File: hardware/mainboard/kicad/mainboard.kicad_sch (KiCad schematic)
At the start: 0 parts

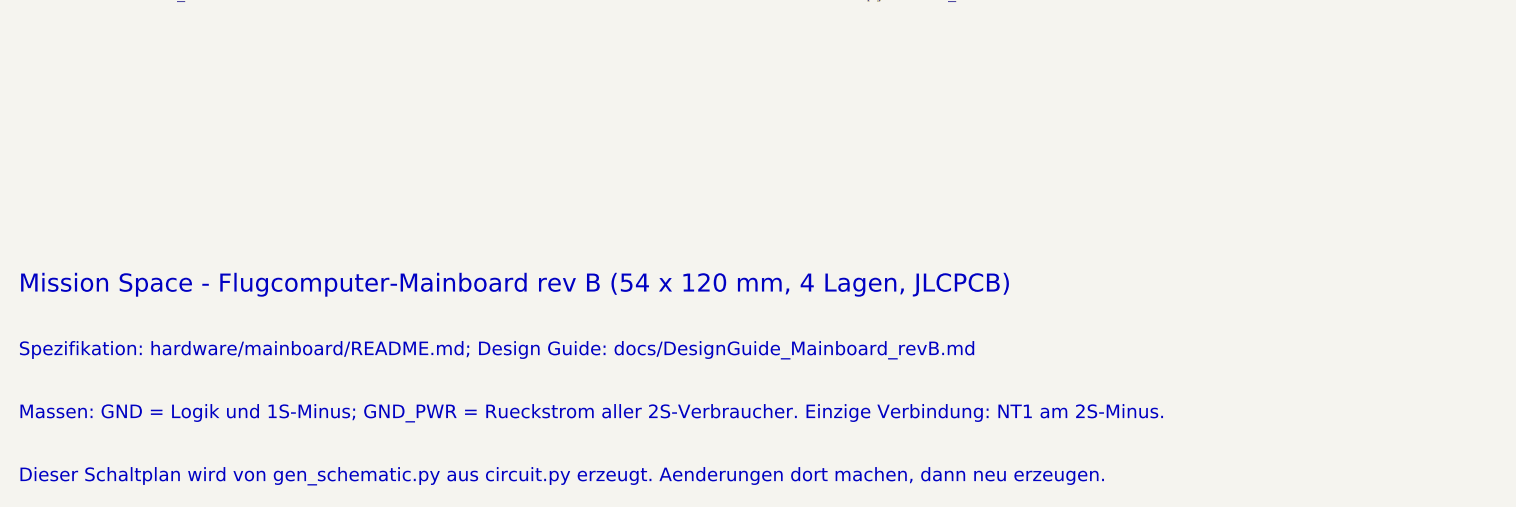
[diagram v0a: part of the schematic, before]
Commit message: Kartonaut: Name, Missionsabzeichen, Bestückungsdruck neu, Lötstopp blau
- Projekt heißt Kartonaut (Karton + Astronaut); Flüge werden hochgezählt, Erstflug = Kartonaut 1
- Abzeichen als Polygone in hardware/mainboard/kicad/logo.py, SVGs in docs/brand/
- spacecode/ -> firmware/, Bodenstation-Repo groundcode -> kartonaut-ground (Links, .gitignore)
- gen_pcb.py silk: Bestückungsdruck nur neu setzen, auf der gerouteten Platine; 1,0 mm Schrift,
  freie Plätze statt Überlappungen, Kurznamen an den Steckern, Testpunkte mit Netznamen,
  kleines Abzeichen vorn; hinten Abzeichen 20 mm und Steckerbelegung
- Stackup JLC04161H-7628 mit blauem Lötstopp im Board, Renders mit Stackup-Farben
- DRC-Druckwarnungen 167 -> 14 (Rest aus Footprint-Umrissen)

Co-Authored-By: Claude Opus 5.5 <noreply@anthropic.com>
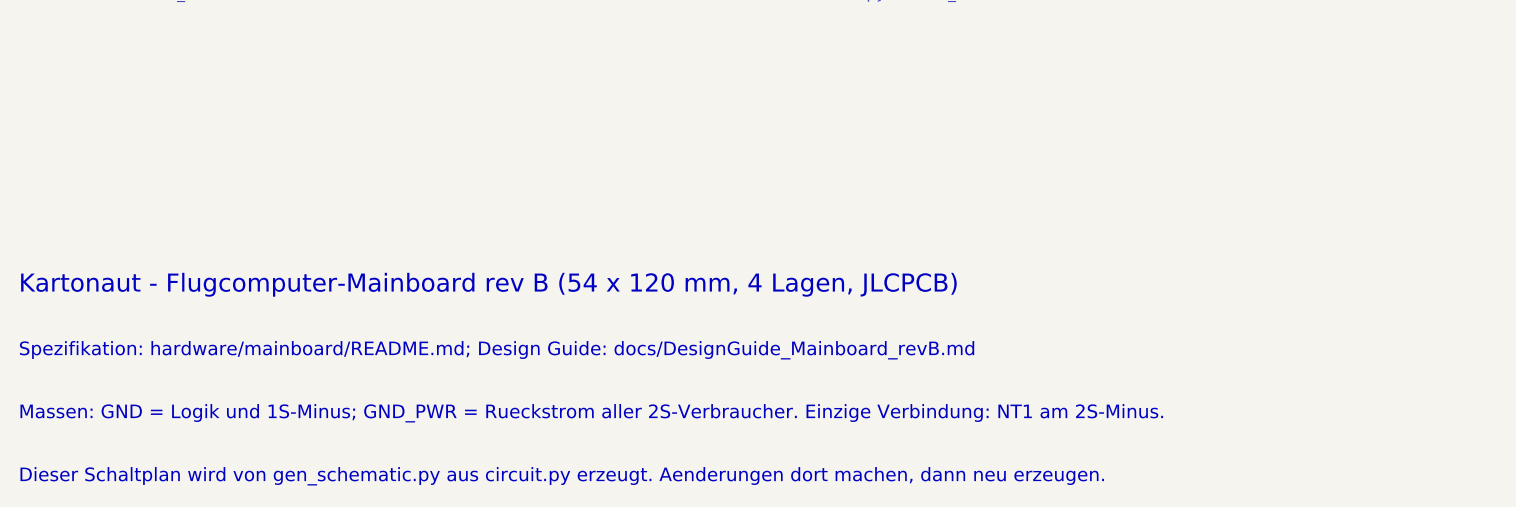
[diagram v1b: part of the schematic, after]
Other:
- note added: "Kartonaut - Flugcomputer-Mainboard rev B (54 x 120 mm, 4 Lagen, JLCPCB)"
- note removed: "Mission Space - Flugcomputer-Mainboard rev B (54 x 120 mm, 4 Lagen, JLCPCB)"
- company: Mission Space -> Kartonaut
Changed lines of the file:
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@@
 		(date "2026-10-21")
 		(rev "B")
-		(company "Mission Space")
+		(company "Kartonaut")
 		(comment 1 "Teensy 4.1, ICM-42688-P, BMP390, E22-400T22S, 1S + 2S")
 	)
@@
 		(effects (font (size 1.27 1.27)) (justify left top))
 	)
-	(text "Mission Space - Flugcomputer-Mainboard rev B (54 x 120 mm, 4 Lagen, JLCPCB)"
+	(text "Kartonaut - Flugcomputer-Mainboard rev B (54 x 120 mm, 4 Lagen, JLCPCB)"
 		(exclude_from_sim no)
 		(at 30 180 0)

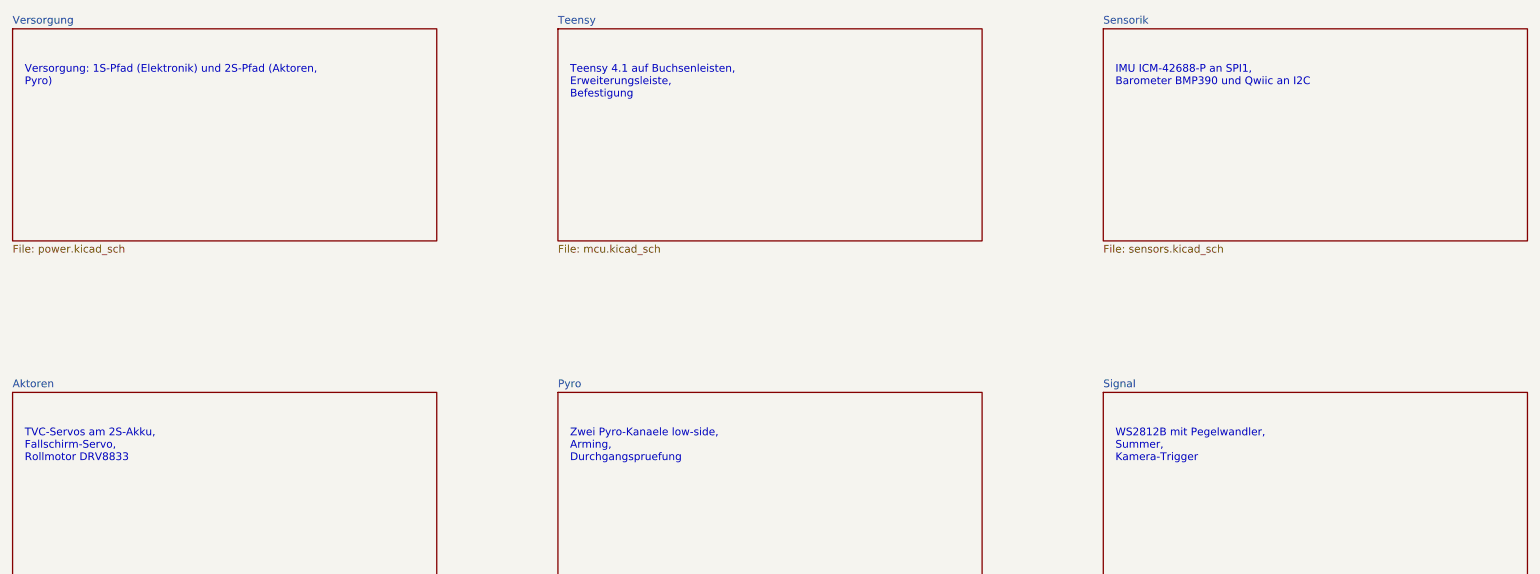
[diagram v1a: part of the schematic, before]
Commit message: Mainboard rev B1: Review A1-A8 und Entscheidungen E1-E10 eingearbeitet, 2S-Pfad als F.Cu-Flaechen, 28 Verbindungen offen
Schaltung (circuit.py, ERC 0, Netzliste gegen README §4 OK): Hold-up hinter D1, EN-Teiler 330k/115k,
P-FET-Lastschalter je Akku, Polyfuse je Akku, Kelvin-Shunt mit INA239 an SPI1, BMP390 an SPI1,
74HC138/74HC4051 mit gemeinsamer Adresse, J_STACK 2x10 mit LDO 3V3_EXP, 1S-Lader MCP73831,
J_CHG2, vier Pyro-Kanaele (3/4 DNP), vierter Servo, alle Servos und Rollmotor an VSERVO,
3V3_SENS, eine WS2812B-Kette, Summer Pin 37, E22 NRST Pin 6; 166 Bauteile.

Platine (gen_pcb.py): neue Platzierung, 2S-Pfad, Pyro-Ausgaenge und VSYS_IN als F.Cu-Flaechen mit
Sperrflaechen fuer Freerouting, Strom-Klasse nur F.Cu, IMU-Zone 5 mm, patch mit Umweg ueber In2.
DRC 0 Fehler, Paritaet 0, kein 2S-Netz auf In2; 28 offene Verbindungen, Liste in kicad/README.md §5.5.
Spezifikation README.md und kicad/README.md auf B1 nachgezogen, review_check_layout.py fuer B1.

Co-Authored-By: Claude Opus 5.5 <noreply@anthropic.com>
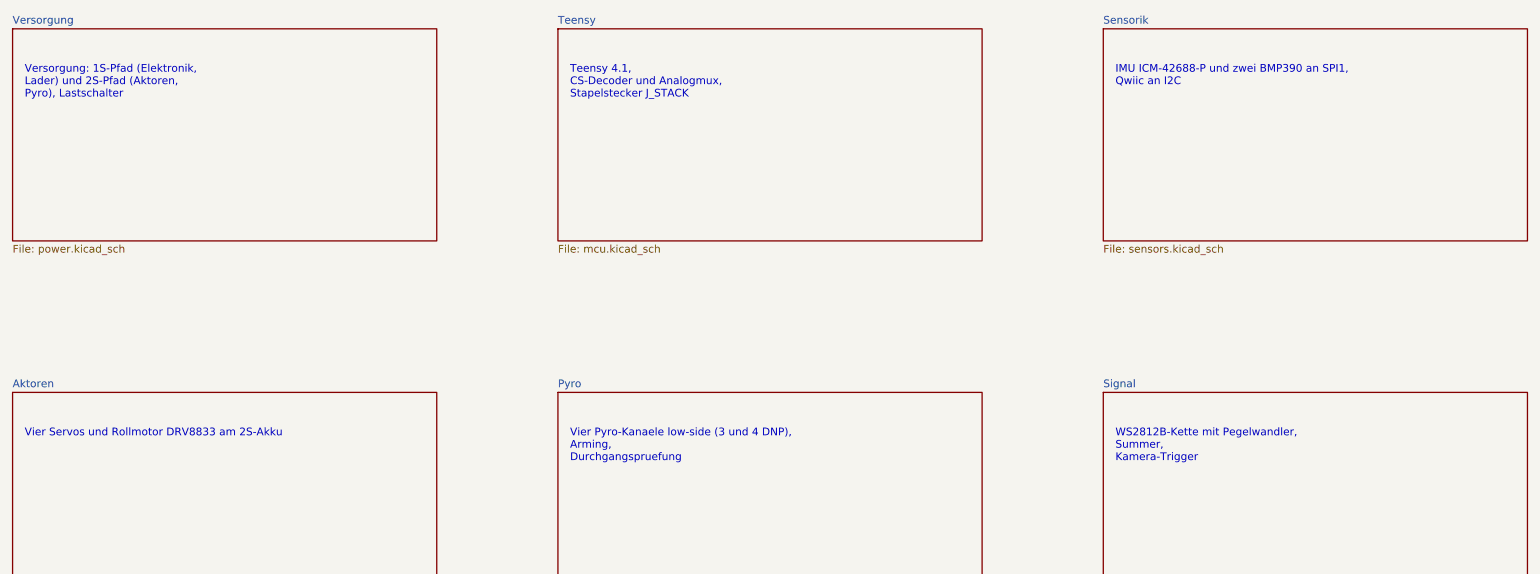
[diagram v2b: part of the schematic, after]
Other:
- note added: "IMU ICM-42688-P und zwei BMP390 an SPI1, Qwiic an I2C"
- note added: "Teensy 4.1, CS-Decoder und Analogmux, Stapelstecker J_STACK"
- note added: "Versorgung: 1S-Pfad (Elektronik, Lader) und 2S-Pfad (Aktoren, Pyro), Lastschalter"
- note added: "Vier Pyro-Kanaele low-side (3 und 4 DNP), Arming, Durchgangspruefung"
- note added: "Vier Servos und Rollmotor DRV8833 am 2S-Akku"
- note added: "WS2812B-Kette mit Pegelwandler, Summer, Kamera-Trigger"
- note removed: "IMU ICM-42688-P an SPI1, Barometer BMP390 und Qwiic an I2C"
- note removed: "TVC-Servos am 2S-Akku, Fallschirm-Servo, Rollmotor DRV8833"
- note removed: "Teensy 4.1 auf Buchsenleisten, Erweiterungsleiste, Befestigung"
- note removed: "Versorgung: 1S-Pfad (Elektronik) und 2S-Pfad (Aktoren, Pyro)"
- note removed: "WS2812B mit Pegelwandler, Summer, Kamera-Trigger"
- note removed: "Zwei Pyro-Kanaele low-side, Arming, Durchgangspruefung"
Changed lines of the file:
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@@
 		)
 	)
-	(text "Versorgung: 1S-Pfad (Elektronik) und 2S-Pfad (Aktoren,\nPyro)"
+	(text "Versorgung: 1S-Pfad (Elektronik,\nLader) und 2S-Pfad (Aktoren,\nPyro), Lastschalter"
 		(exclude_from_sim no)
 		(at 32 56 0)
@@
 		)
 	)
-	(text "Teensy 4.1 auf Buchsenleisten,\nErweiterungsleiste,\nBefestigung"
+	(text "Teensy 4.1,\nCS-Decoder und Analogmux,\nStapelstecker J_STACK"
 		(exclude_from_sim no)
 		(at 122 56 0)
@@
 		)
 	)
-	(text "IMU ICM-42688-P an SPI1,\nBarometer BMP390 und Qwiic an I2C"
+	(text "IMU ICM-42688-P und zwei BMP390 an SPI1,\nQwiic an I2C"
 		(exclude_from_sim no)
 		(at 212 56 0)
@@
 		)
 	)
-	(text "TVC-Servos am 2S-Akku,\nFallschirm-Servo,\nRollmotor DRV8833"
+	(text "Vier Servos und Rollmotor DRV8833 am 2S-Akku"
 		(exclude_from_sim no)
 		(at 32 116 0)
@@
 		)
 	)
-	(text "Zwei Pyro-Kanaele low-side,\nArming,\nDurchgangspruefung"
+	(text "Vier Pyro-Kanaele low-side (3 und 4 DNP),\nArming,\nDurchgangspruefung"
 		(exclude_from_sim no)
 		(at 122 116 0)
@@
 		)
 	)
-	(text "WS2812B mit Pegelwandler,\nSummer,\nKamera-Trigger"
+	(text "WS2812B-Kette mit Pegelwandler,\nSummer,\nKamera-Trigger"
 		(exclude_from_sim no)
 		(at 212 116 0)

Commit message: Schaltplan: Blattname Sensorik mit LSM6DSV16X auch im Wurzelblatt
Co-Authored-By: Claude Fable 5.1 <noreply@anthropic.com>
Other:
- note added: "IMU LSM6DSV16X und zwei BMP390 an SPI1, I2C-Sensoren und Qwiic"
- note removed: "IMU ICM-42688-P und zwei BMP390 an SPI1, Qwiic an I2C"
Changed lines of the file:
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@@
 		)
 	)
-	(text "IMU ICM-42688-P und zwei BMP390 an SPI1,\nQwiic an I2C"
+	(text "IMU LSM6DSV16X und zwei BMP390 an SPI1,\nI2C-Sensoren und Qwiic"
 		(exclude_from_sim no)
 		(at 212 56 0)
